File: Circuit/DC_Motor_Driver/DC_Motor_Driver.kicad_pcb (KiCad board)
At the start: 2 copper layers, 57.5 x 17.7 mm, 13 parts, among them J1 Conn_01x03_Socket, Q1 S8050, Q2 S8050, Q3 S8550, Q4 S8050, Q5 IRF540N

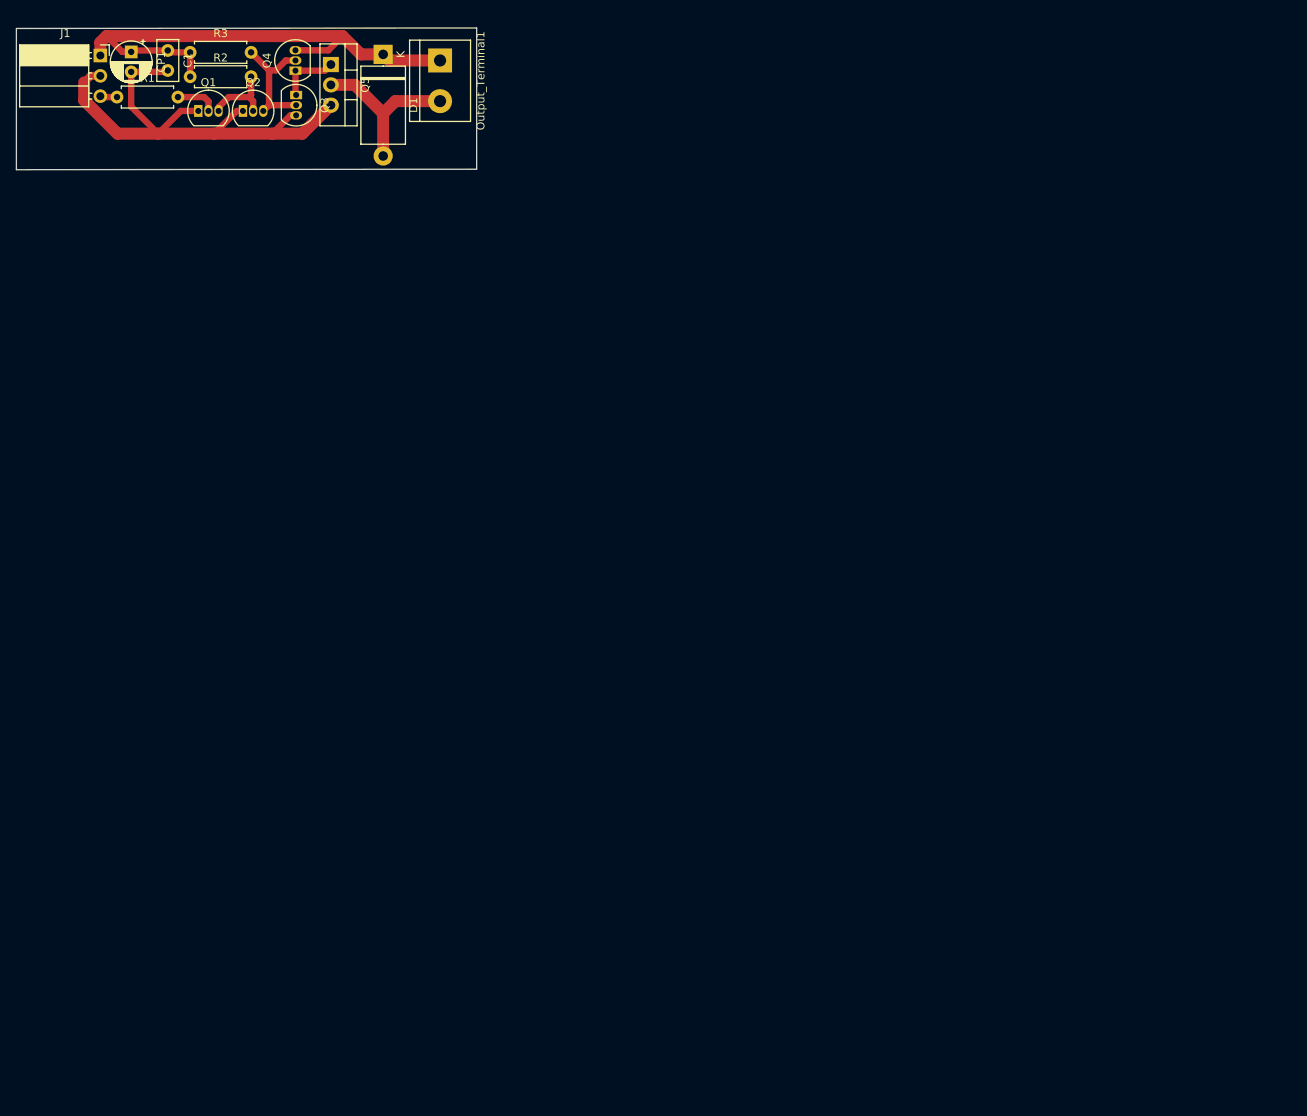
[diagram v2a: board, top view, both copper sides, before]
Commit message: DC Motor Driver Circuit fine tuning for manufacturing
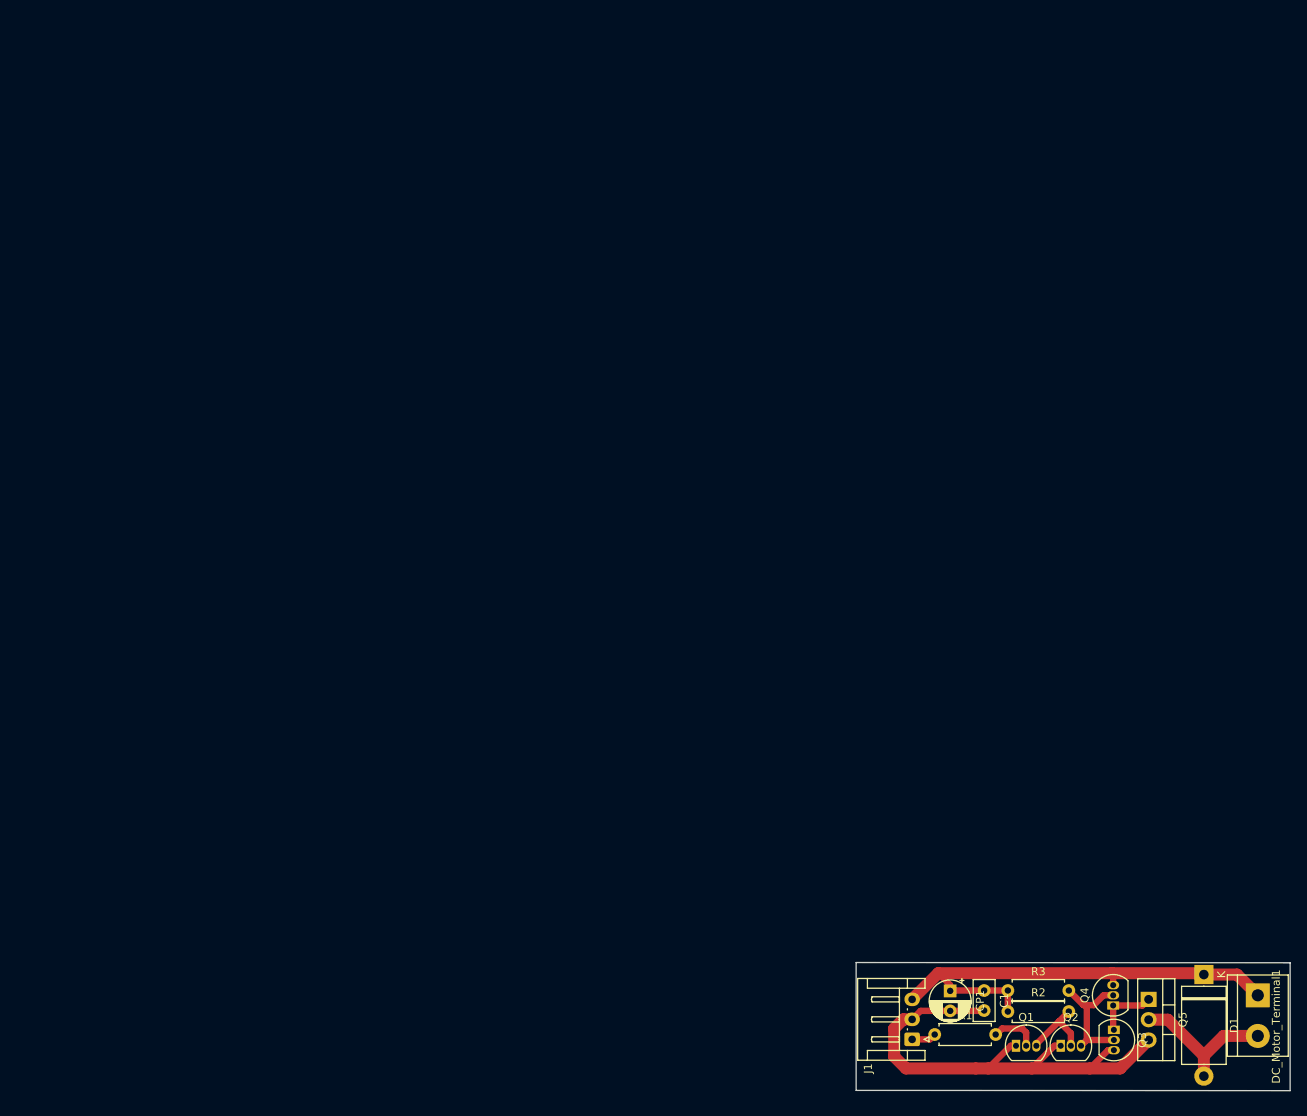
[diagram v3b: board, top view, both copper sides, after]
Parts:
- J1: footprint Connector_PinSocket_2.54mm:PinSocket_1x03_P2.54mm_Horizontal -> Connector_JST:JST_EH_S3B-EH_1x03_P2.50mm_Horizontal
- moved J1 159.4 mm to (122.0, 106.1), turned to 90 degrees
- moved CP1 155.7 mm to (126.8, 100.0)
- moved C1 155.6 mm to (131.0, 100.0)
- moved R3 155.6 mm to (134.0, 100.0)
- moved R1 155.5 mm to (124.8, 105.5)
- moved DC_Motor_Terminal1 155.3 mm to (165.2, 100.6)
- moved Q1 155.3 mm to (135.0, 106.9)
- moved Q2 155.3 mm to (140.6, 106.9)
- moved Q3 155.3 mm to (147.2, 104.9)
- moved Q4 155.3 mm to (147.1, 101.9)
- moved R2 155.3 mm to (134.0, 102.6)
- moved Q5 155.3 mm to (151.6, 101.1)
- moved D1 154.1 mm to (158.5, 98.0)
- renumbered Output_Terminal1 to DC_Motor_Terminal1
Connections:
- J1 pad 1: +12V -> Control_Signal
- J1 pad 3: Control_Signal -> +12V
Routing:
- net +12V: track 67.2 -> 60.5 mm
- net GND: track 67.3 -> 63.0 mm
- net Net-(D1-A): track 21.1 -> 19.1 mm
- net Control_Signal: track 2.12 -> 3.07 mm
- net Net-(Q1-B): track 5.23 -> 5.98 mm
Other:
- board size 57.5 x 17.7 mm -> 54.2 x 16 mm
